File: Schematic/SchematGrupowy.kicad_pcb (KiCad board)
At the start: 2 copper layers, 62 parts, among them J1 USB_C_Receptacle_USB2.0_14P, J2 Conn_01x04_Pin, J3 Conn_01x04_Pin, J4 Micro_SD_Card_Det1, J5 LCD, J7 Programing, J8 Programing, SW1 SW_Wuerth_450301014042, SW2 RotaryEncoder_Switch_MP, U1 STM32F411CEUx, U2 BMI160, U3 NEO-M8N, U4 TP4056-42-ESOP8, U5 MCP1700-3302E, U6 STM32F303K8Tx

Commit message: Apply final touches to PCB design
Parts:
- removed D3, D4, D5, D6: LED, LED_SMD:LED_0805_2012Metric_Pad1.15x1.40mm_HandSolder
- removed R11, R12, R13, R14: 470, Resistor_SMD:R_0805_2012Metric_Pad1.20x1.40mm_HandSolder
- added REF**: MountingHole_2.1mm, MountingHole:MountingHole_2.1mm, F.Cu at (235.0, 144.5)
- added REF**: MountingHole_2.1mm, MountingHole:MountingHole_2.1mm, F.Cu at (145.5, 144.5)
- added REF**: MountingHole_2.1mm, MountingHole:MountingHole_2.1mm, F.Cu at (145.5, 61.5)
- added REF**: MountingHole_2.1mm, MountingHole:MountingHole_2.1mm, F.Cu at (235.0, 61.5)
- BT1, C1, C2, C3, J1, J4, R1, R18, R19, R2, R21, R22, R3, R4, R5, U4, U5: moved to B.Cu
- J2: value Conn_01x04_Pin -> UART1
- J3: value Conn_01x04_Pin -> UART2
- J7: value Programing -> Programing1
- J8: value Programing -> Programing2
- moved J1 52.9 mm to (146.5, 91.8), turned to 90 degrees
- moved C15 47.8 mm to (197.0, 122.5), turned to -90 degrees
- moved U2 46.3 mm to (179.5, 108.5)
- moved C14 46.0 mm to (198.0, 105.5), turned to 90 degrees
- moved C8 45.6 mm to (190.0, 84.0), turned to -90 degrees
- moved R17 45.6 mm to (197.5, 129.5), turned to 180 degrees
- moved C20 45.4 mm to (197.5, 126.5), turned to 180 degrees
- moved J4 45.0 mm to (158.5, 138.0), turned to 180 degrees
- moved C17 44.8 mm to (194.5, 121.5), turned to -90 degrees
- moved C16 44.5 mm to (192.0, 121.5), turned to -90 degrees
- moved C19 43.4 mm to (193.5, 126.5)
- moved U4 43.0 mm to (164.6, 97.6), turned to -90 degrees
- moved R6 42.7 mm to (182.5, 85.0)
- moved R16 42.4 mm to (193.5, 129.5)
- moved C18 41.5 mm to (189.0, 126.5)
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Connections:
- net SD_CLK renamed MCU_CLK
- net SD_MOSI renamed MCU_MOSI
- J3 pad 3: UART2_RX -> UART2_RXD
- R7 pad 1: BMI_SDA -> VCC
- R7 pad 2: VCC -> BMI_SDA
- R8 pad 1: BMI_SCL -> VCC
- R8 pad 2: VCC -> BMI_SCL
- U1 pad 32: MK12_TXD2 -> MK12_TXDRXD
- U1 pad 33: MK12_RXD2 -> MK12_RXDTXD
- U2 pad 13: VCC -> BMI_SDA
- U2 pad 14: VCC -> BMI_SCL
- U3 pad 9: VCC -> unconnected-(U3-VCC_RF-Pad9)
- U6 pad 19: MK12_TXD2 -> MK12_RXDTXD
- U6 pad 20: MK12_RXD2 -> MK12_TXDRXD
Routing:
- net VCC: track 0.00 -> 361.8 mm, vias 0 -> 15
- net MCU_MOSI: track 0.00 -> 114.7 mm, vias 0 -> 3
- net SD_CS: track 0.00 -> 103.8 mm, vias 0 -> 2
- net Net-(BT1-+): track 0.00 -> 99.5 mm
- net GND: track 0.00 -> 90.9 mm
- net SD_DET: track 0.00 -> 87.7 mm, vias 0 -> 2
- net SD_MISO: track 0.00 -> 81.8 mm, vias 0 -> 2
- net MCU_CLK: track 0.00 -> 71.6 mm, vias 0 -> 2
- net +5V: track 0.00 -> 65.9 mm, vias 0 -> 2
- net TFT_RST: track 0.00 -> 47.2 mm, vias 0 -> 1
- net SWCLK_2: track 0.00 -> 44.0 mm, vias 0 -> 1
- net SWDIO_2: track 0.00 -> 43.4 mm, vias 0 -> 1
- net TFT_DC: track 0.00 -> 43.4 mm, vias 0 -> 1
- net TFT_CS: track 0.00 -> 38.3 mm, vias 0 -> 1
- net BMI_SDA: track 0.00 -> 36.8 mm, vias 0 -> 2
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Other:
- board outline added: 94.5 x 88 mm

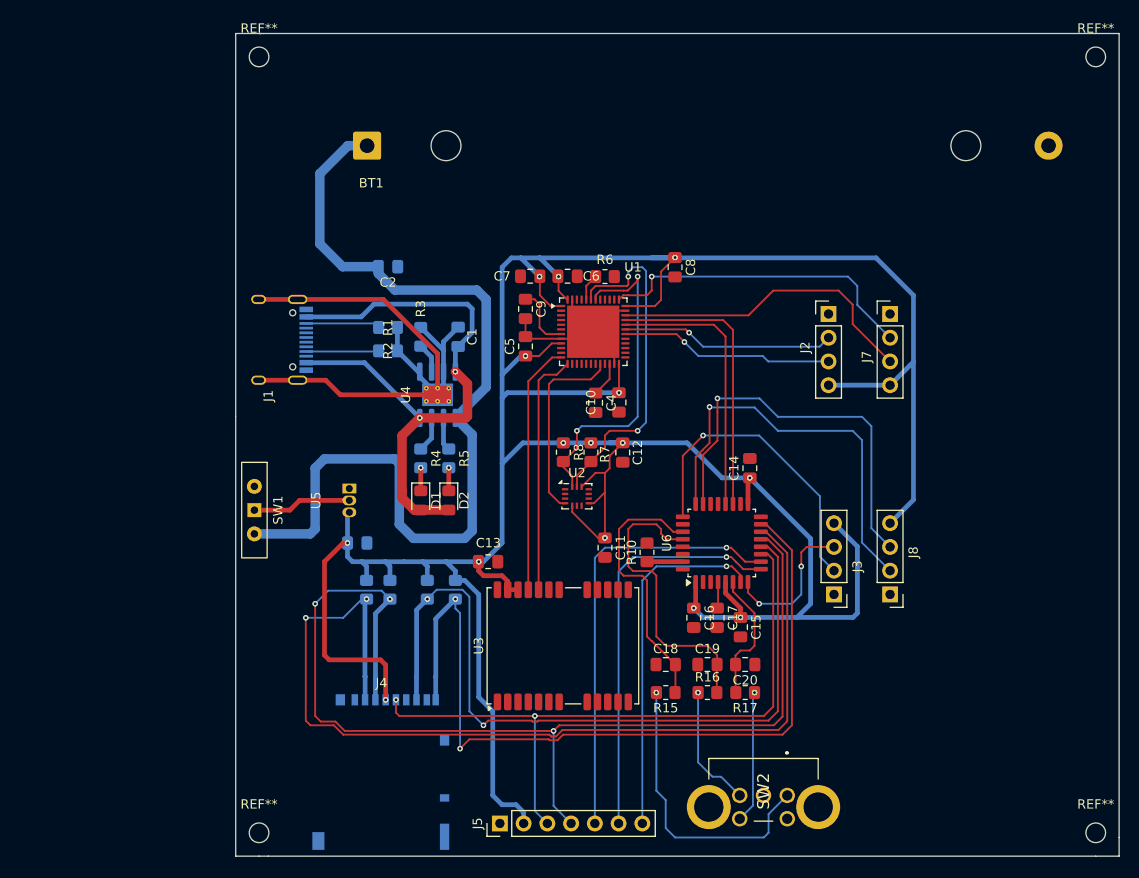
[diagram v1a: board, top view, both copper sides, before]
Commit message: Resolve DRC issues and pour ground planes
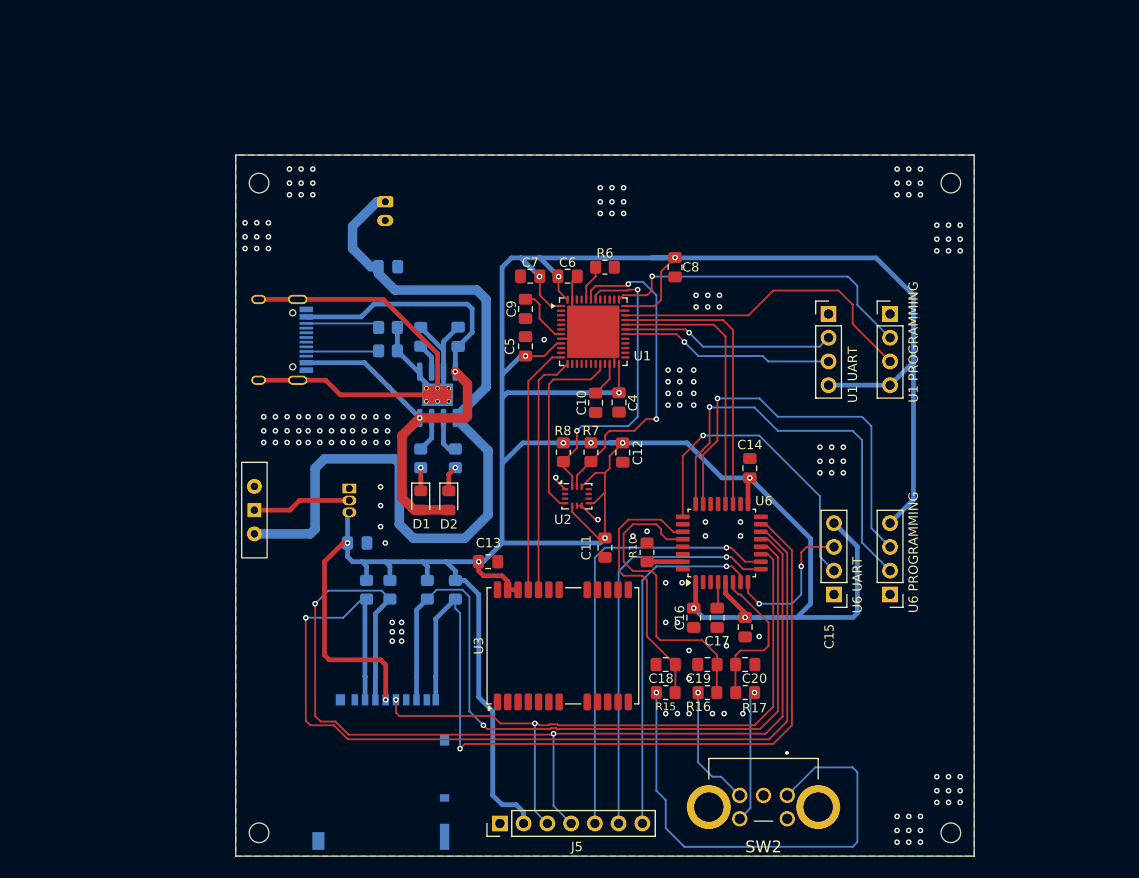
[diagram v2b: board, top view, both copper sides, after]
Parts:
- BT1: footprint Battery:BatteryHolder_MPD_BK-18650-PC2 -> Connector_JST:JST_PH_S2B-PH-K_1x02_P2.00mm_Horizontal
- U1 PROGRAMMING: renamed from J7
- U1 UART: renamed from J2
- U6 PROGRAMMING: renamed from J8
- U6 UART: renamed from J3
- moved REF** 20.6 mm to (219.5, 75.0)
- moved REF** 15.5 mm to (219.5, 144.5)
- moved REF** 13.5 mm to (145.5, 75.0)
- moved BT1 6.31 mm to (159.0, 77.0), turned to -90 degrees
- moved R6 1.00 mm to (182.5, 84.0)
- moved R5 0.71 mm to (166.5, 104.4)
- moved C15 0.50 mm to (197.5, 122.5)
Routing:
- net Net-(R15-Pad2): track 31.4 -> 52.9 mm
- net VCC: track 361.8 -> 374.7 mm
- net Net-(BT1-+): track 99.5 -> 90.3 mm
- net SW1: track 14.2 -> 16.5 mm
- net BMI_SCL: track 35.1 -> 32.9 mm
- net GND: track 90.9 -> 92.6 mm, vias 0 -> 159
- net BMI_SDA: track 36.8 -> 35.2 mm
- net Net-(U1-BOOT0): track 2.88 -> 3.88 mm
- net Net-(U4-~{STDBY}): track 3.56 -> 4.26 mm
- net Net-(U1-NRST): track 6.82 -> 6.26 mm
- net SD_MISO: track 81.8 -> 82.2 mm, vias 2 -> 1
- net SD_CS: track 103.8 -> 104.1 mm, vias 2 -> 1
- net SD_DET: track 87.7 -> 87.6 mm, vias 2 -> 1
- net MCU_MOSI: vias 3 -> 2
- added copper zone on B.Cu, net GND
- added copper zone on F.Cu, net GND
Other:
- board size 94.5 x 88 mm -> 79 x 75 mm

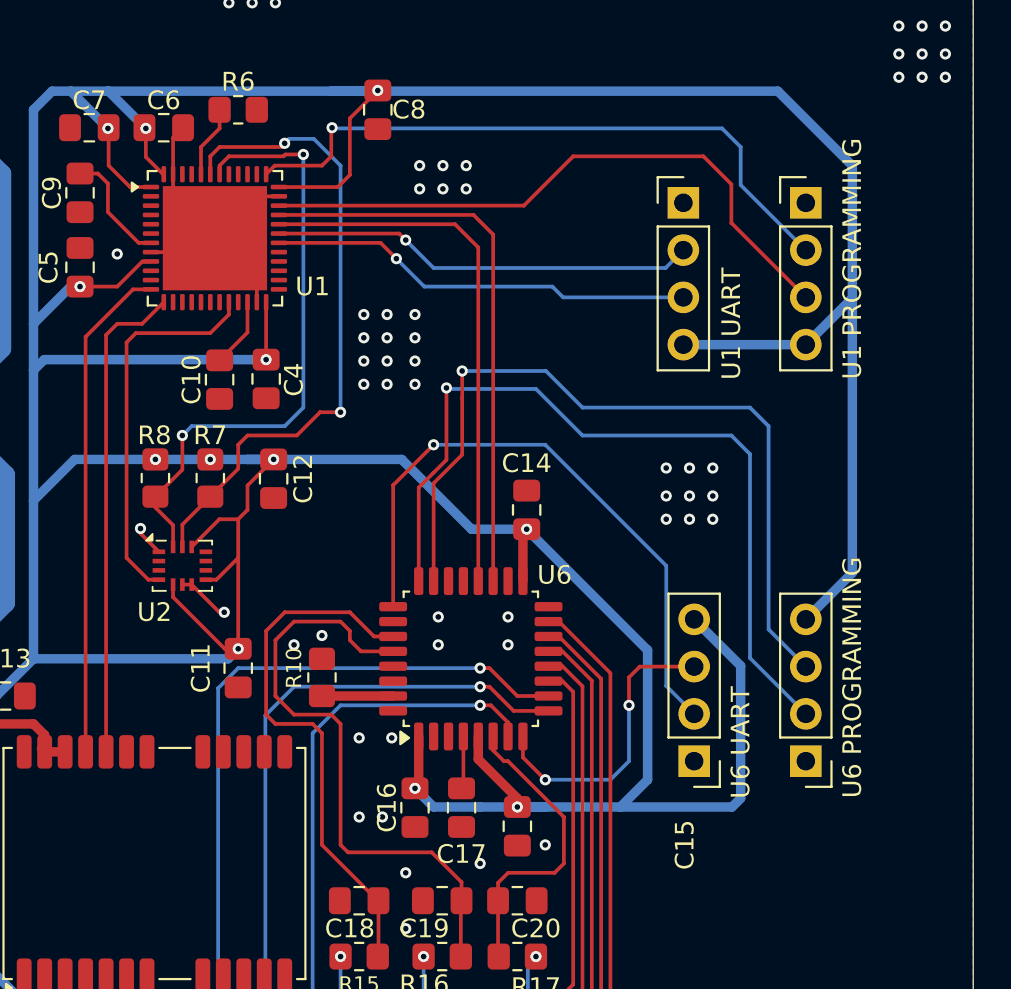
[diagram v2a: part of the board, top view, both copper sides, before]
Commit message: Added descriptions for programming/uart pins
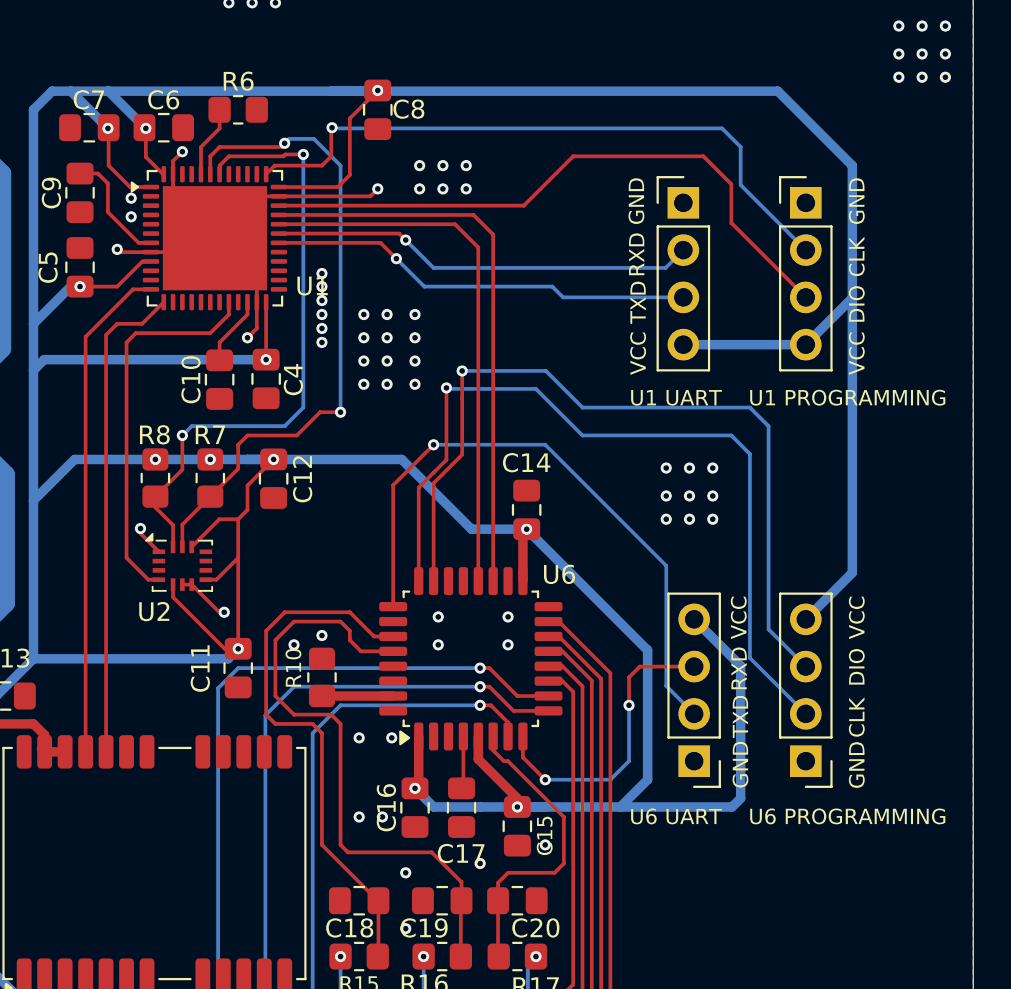
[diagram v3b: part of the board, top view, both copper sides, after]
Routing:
- net GND: track 92.6 -> 100.8 mm, vias 159 -> 170
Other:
- board text added: "CLK"
- board text added: "DIO"
- board text added: "GND"
- board text added: "RXD"
- board text added: "TXD"
- board text added: "VCC"

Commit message: Added Gerbres,screens and footprint fixes
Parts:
- J2: renamed from U1 UART
- J3: renamed from U6 UART
- J7: renamed from U1 PROGRAMMING
- J8: renamed from U6 PROGRAMMING
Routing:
- net GND: track 100.8 -> 84.6 mm
